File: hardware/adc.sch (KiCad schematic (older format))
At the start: 8 parts, among them U401 MCP3424, U402 FDC6301N, U403 MCP3424

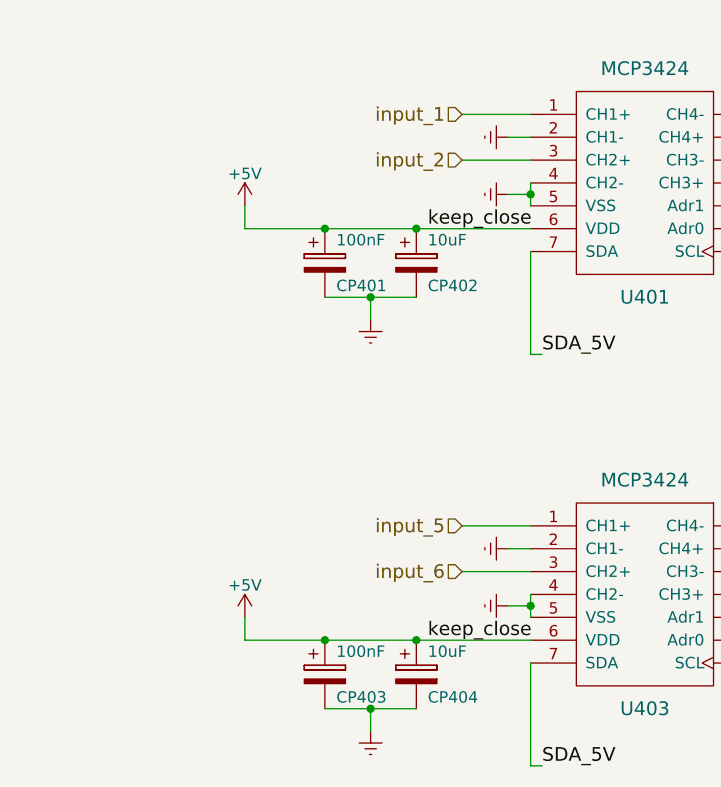
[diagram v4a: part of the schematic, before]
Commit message: finalized most footprints and nets.
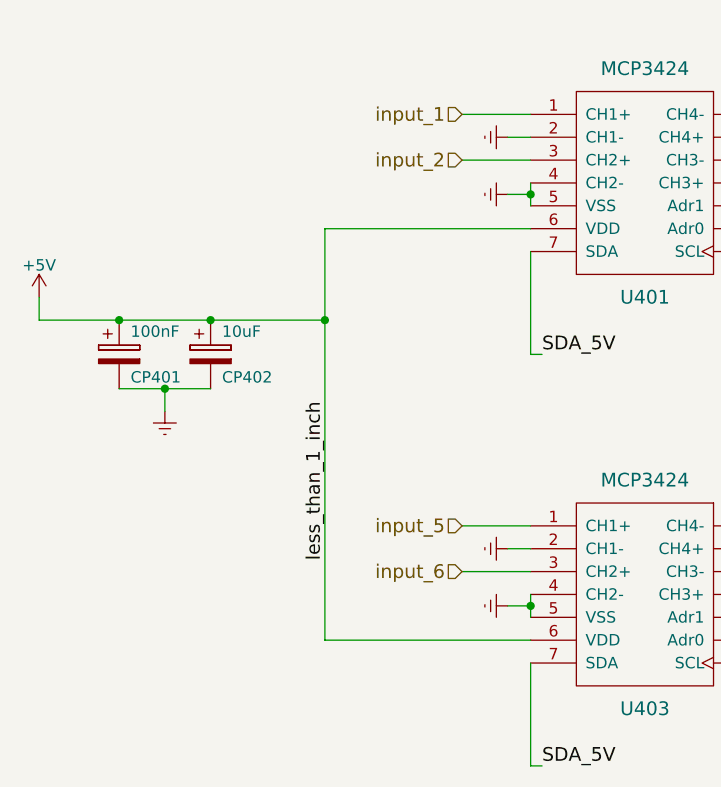
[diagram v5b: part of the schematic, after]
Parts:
- removed CP403: 100nF, Capacitors_THT:CP_Radial_D5.0mm_P2.00mm, symbol CP
- removed CP404: 10uF, Capacitors_THT:CP_Radial_D5.0mm_P2.00mm, symbol CP
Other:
- moved on the sheet: CP401, CP402
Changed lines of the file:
@@
 L +5V #PWR047
 U 1 1 5BE37FBA
-P 1900 1900
-F 0 "#PWR047" H 1900 1750 50  0001 C CNN
-F 1 "+5V" H 1900 2040 50  0000 C CNN
-F 2 "" H 1900 1900 50  0000 C CNN
-F 3 "" H 1900 1900 50  0000 C CNN
-	1    1900 1900
+P 1000 2300
+F 0 "#PWR047" H 1000 2150 50  0001 C CNN
+F 1 "+5V" H 1000 2440 50  0000 C CNN
+F 2 "" H 1000 2300 50  0000 C CNN
+F 3 "" H 1000 2300 50  0000 C CNN
+	1    1000 2300
 	1    0    0    -1
 $EndComp
@@
 L Earth #PWR048
 U 1 1 5BE38215
-P 2450 2400
-F 0 "#PWR048" H 2450 2150 50  0001 C CNN
-F 1 "Earth" H 2450 2250 50  0001 C CNN
-F 2 "" H 2450 2400 50  0000 C CNN
-F 3 "" H 2450 2400 50  0000 C CNN
-	1    2450 2400
+P 1550 2800
+F 0 "#PWR048" H 1550 2550 50  0001 C CNN
+F 1 "Earth" H 1550 2650 50  0001 C CNN
+F 2 "" H 1550 2800 50  0000 C CNN
+F 3 "" H 1550 2800 50  0000 C CNN
+	1    1550 2800
 	1    0    0    -1
 $EndComp
@@
 L CP CP402
 U 1 1 5BE3829F
-P 2650 2150
-F 0 "CP402" H 2700 2050 50  0000 L CNN
-F 1 "10uF" H 2700 2250 50  0000 L CNN
-F 2 "Capacitors_THT:CP_Radial_D5.0mm_P2.00mm" H 2688 2000 50  0001 C CNN
-F 3 "" H 2650 2150 50  0000 C CNN
-	1    2650 2150
+P 1750 2550
+F 0 "CP402" H 1800 2450 50  0000 L CNN
+F 1 "10uF" H 1800 2650 50  0000 L CNN
+F 2 "Capacitors_THT:CP_Radial_D5.0mm_P2.00mm" H 1788 2400 50  0001 C CNN
+F 3 "" H 1750 2550 50  0000 C CNN
+	1    1750 2550
 	1    0    0    -1
 $EndComp
@@
 L CP CP401
 U 1 1 5BE382F8
-P 2250 2150
-F 0 "CP401" H 2300 2050 50  0000 L CNN
-F 1 "100nF" H 2300 2250 50  0000 L CNN
-F 2 "Capacitors_THT:CP_Radial_D5.0mm_P2.00mm" H 2288 2000 50  0001 C CNN
-F 3 "" H 2250 2150 50  0000 C CNN
-	1    2250 2150
-	1    0    0    -1
-$EndComp
-Wire Wire Line
-	2250 2300 2650 2300
-Wire Wire Line
-	1900 2000 3150 2000
-Connection ~ 2650 2000
-Text Label 2700 2000 0    60   ~ 0
-keep_close
-Connection ~ 2250 2000
-Wire Wire Line
-	2450 2400 2450 2300
-Connection ~ 2450 2300
+P 1350 2550
+F 0 "CP401" H 1400 2450 50  0000 L CNN
+F 1 "100nF" H 1400 2650 50  0000 L CNN
+F 2 "Capacitors_THT:CP_Radial_D5.0mm_P2.00mm" H 1388 2400 50  0001 C CNN
+F 3 "" H 1350 2550 50  0000 C CNN
+	1    1350 2550
+	1    0    0    -1
+$EndComp
+Wire Wire Line
+	1350 2700 1750 2700
+Wire Wire Line
+	1000 2400 2250 2400
+Connection ~ 1750 2400
+Connection ~ 1350 2400
+Wire Wire Line
+	1550 2800 1550 2700
+Connection ~ 1550 2700
 Wire Wire Line
 	3150 1800 3150 1900
@@
 Connection ~ 3150 1850
 Wire Wire Line
-	1900 2000 1900 1900
-$Comp
-L Earth #PWR049
-U 1 1 5BE44E1F
-P 2450 4200
-F 0 "#PWR049" H 2450 3950 50  0001 C CNN
-F 1 "Earth" H 2450 4050 50  0001 C CNN
-F 2 "" H 2450 4200 50  0000 C CNN
-F 3 "" H 2450 4200 50  0000 C CNN
-	1    2450 4200
-	1    0    0    -1
-$EndComp
-$Comp
-L CP CP404
-U 1 1 5BE44E25
-P 2650 3950
-F 0 "CP404" H 2700 3850 50  0000 L CNN
-F 1 "10uF" H 2700 4050 50  0000 L CNN
-F 2 "Capacitors_THT:CP_Radial_D5.0mm_P2.00mm" H 2688 3800 50  0001 C CNN
-F 3 "" H 2650 3950 50  0000 C CNN
-	1    2650 3950
-	1    0    0    -1
-$EndComp
-$Comp
-L CP CP403
-U 1 1 5BE44E2C
-P 2250 3950
-F 0 "CP403" H 2300 3850 50  0000 L CNN
-F 1 "100nF" H 2300 4050 50  0000 L CNN
-F 2 "Capacitors_THT:CP_Radial_D5.0mm_P2.00mm" H 2288 3800 50  0001 C CNN
-F 3 "" H 2250 3950 50  0000 C CNN
-	1    2250 3950
-	1    0    0    -1
-$EndComp
-Wire Wire Line
-	2250 4100 2650 4100
-Wire Wire Line
-	1900 3800 3150 3800
-Connection ~ 2650 3800
-Text Label 2700 3800 0    60   ~ 0
-keep_close
-Connection ~ 2250 3800
-Wire Wire Line
-	2450 4200 2450 4100
-Connection ~ 2450 4100
-Wire Wire Line
-	1900 3800 1900 3700
+	1000 2400 1000 2300
 Wire Wire Line
 	3150 3600 3150 3700
@@
 Connection ~ 3150 3650
 $Comp
-L +5V #PWR050
-U 1 1 5BE44ED3
-P 1900 3700
-F 0 "#PWR050" H 1900 3550 50  0001 C CNN
-F 1 "+5V" H 1900 3840 50  0000 C CNN
-F 2 "" H 1900 3700 50  0000 C CNN
-F 3 "" H 1900 3700 50  0000 C CNN
-	1    1900 3700
-	1    0    0    -1
-$EndComp
-$Comp
-L +3.3V #PWR051
+L +3.3V #PWR049
 U 1 1 5BE6308C
 P 5350 2250
-F 0 "#PWR051" H 5350 2100 50  0001 C CNN
+F 0 "#PWR049" H 5350 2100 50  0001 C CNN
 F 1 "+3.3V" H 5350 2390 50  0000 C CNN
 F 2 "" H 5350 2250 50  0000 C CNN
@@
 $EndComp
 $Comp
-L +5V #PWR052
+L +5V #PWR050
 U 1 1 5BE630B5
 P 6500 900
-F 0 "#PWR052" H 6500 750 50  0001 C CNN
+F 0 "#PWR050" H 6500 750 50  0001 C CNN
 F 1 "+5V" H 6500 1040 50  0000 C CNN
 F 2 "" H 6500 900 50  0000 C CNN
@@
 	6300 2450 7250 2450
 $Comp
-L +3.3V #PWR053
+L +3.3V #PWR051
 U 1 1 5BE63D55
 P 6500 1550
-F 0 "#PWR053" H 6500 1400 50  0001 C CNN
+F 0 "#PWR051" H 6500 1400 50  0001 C CNN
 F 1 "+3.3V" H 6500 1690 50  0000 C CNN
 F 2 "" H 6500 1550 50  0000 C CNN
@@
 SDA_5V
 $Comp
-L +5V #PWR054
+L +5V #PWR052
 U 1 1 5BE65F8B
 P 4150 1900
-F 0 "#PWR054" H 4150 1750 50  0001 C CNN
+F 0 "#PWR052" H 4150 1750 50  0001 C CNN
 F 1 "+5V" H 4150 2040 50  0000 C CNN
 F 2 "" H 4150 1900 50  0000 C CNN
@@
 $EndComp
 $Comp
-L +5V #PWR055
+L +5V #PWR053
 U 1 1 5BE65FBD
 P 4150 3800
-F 0 "#PWR055" H 4150 3650 50  0001 C CNN
+F 0 "#PWR053" H 4150 3650 50  0001 C CNN
 F 1 "+5V" H 4150 3940 50  0000 C CNN
 F 2 "" H 4150 3800 50  0000 C CNN
@@
 $EndComp
 $Comp
-L Earth #PWR056
+L Earth #PWR054
 U 1 1 5BE65FEA
 P 4150 2000
-F 0 "#PWR056" H 4150 1750 50  0001 C CNN
+F 0 "#PWR054" H 4150 1750 50  0001 C CNN
 F 1 "Earth" H 4150 1850 50  0001 C CNN
 F 2 "" H 4150 2000 50  0000 C CNN
@@
 $EndComp
 $Comp
-L Earth #PWR057
+L Earth #PWR055
 U 1 1 5BE6601E
 P 4150 3700
-F 0 "#PWR057" H 4150 3450 50  0001 C CNN
+F 0 "#PWR055" H 4150 3450 50  0001 C CNN
 F 1 "Earth" H 4150 3550 50  0001 C CNN
 F 2 "" H 4150 3700 50  0000 C CNN
@@
 	0    -1   -1   0
 $EndComp
+Wire Wire Line
+	2250 3800 3150 3800
+Text Label 2250 3450 1    60   ~ 0
+less_than_1_inch
+Wire Wire Line
+	3150 2000 2250 2000
+Wire Wire Line
+	2250 2000 2250 3800
+Connection ~ 2250 2400
 $EndSCHEMATC
